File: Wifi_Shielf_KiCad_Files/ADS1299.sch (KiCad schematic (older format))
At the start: 20 parts, among them U9 ADS1299

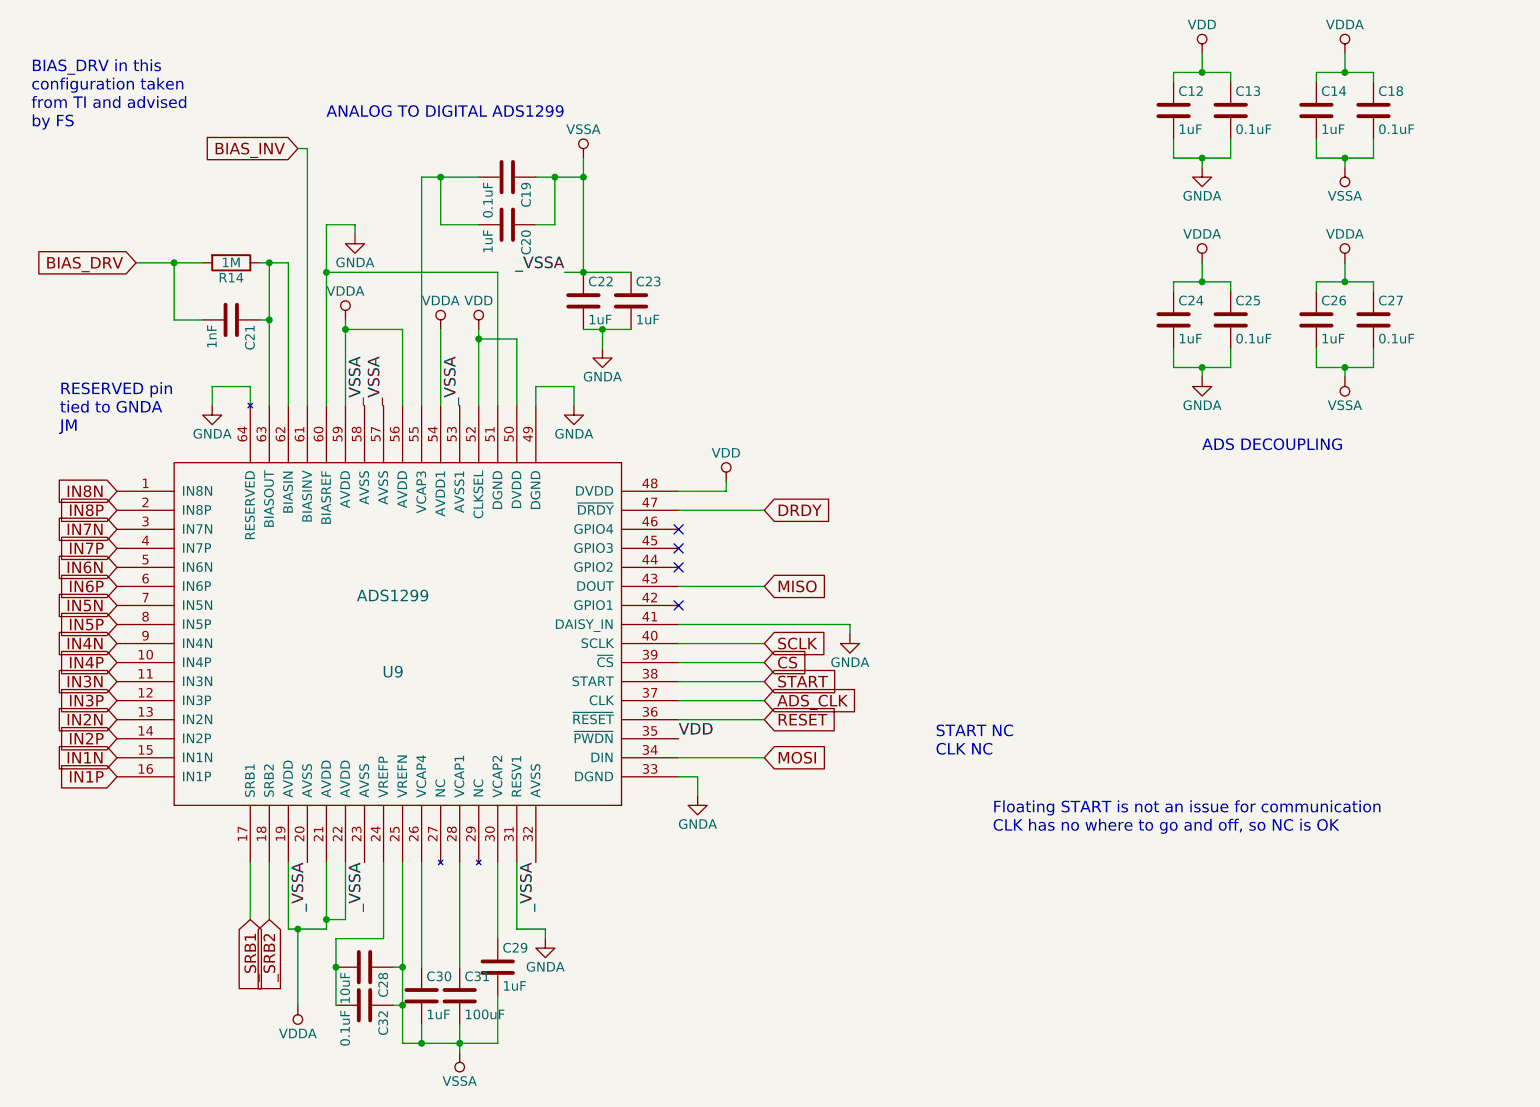
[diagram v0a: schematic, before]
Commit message: FIX: Finish DRC
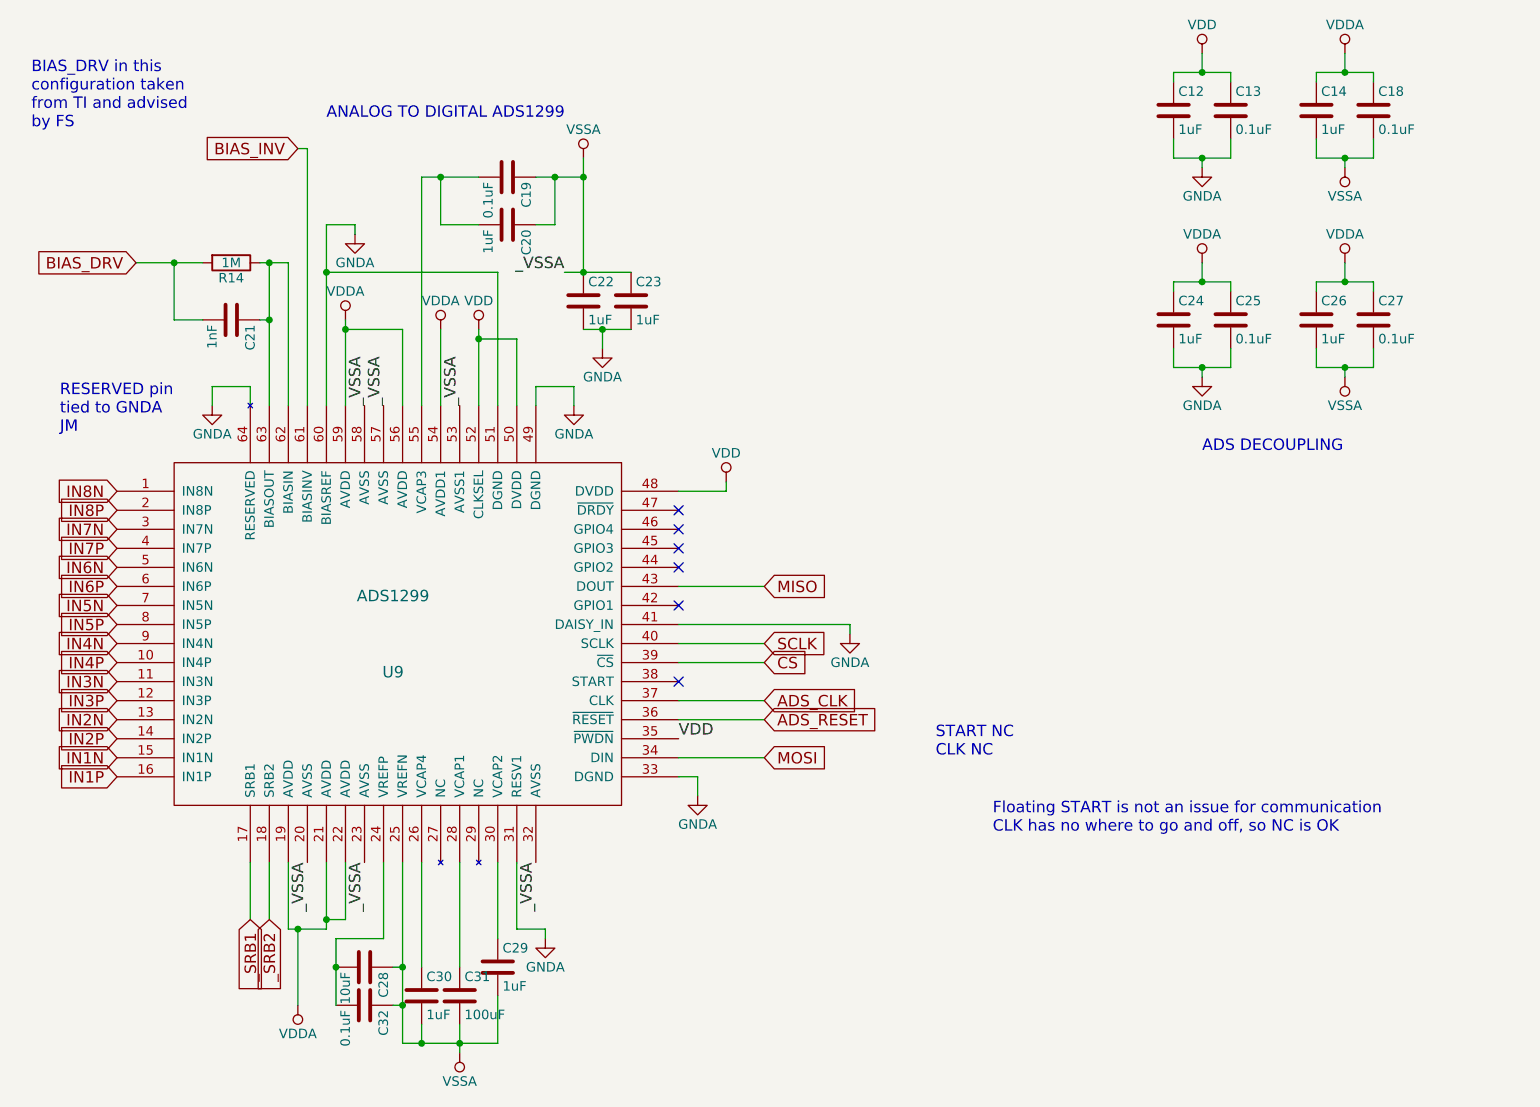
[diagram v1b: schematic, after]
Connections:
- net DRDY: no longer names the net of U9.47 (~DRDY~)
- net RESET renamed ADS_RESET
- net START: no longer names the net of U9.38 (START)
- no-connect marks 4 -> 6
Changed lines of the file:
@@
 $EndComp
 $Comp
-L GNDA #PWR36
+L GNDA #PWR031
 U 1 1 59A60DC4
 P 4050 2200
-F 0 "#PWR36" H 4050 1950 50  0001 C CNN
+F 0 "#PWR031" H 4050 1950 50  0001 C CNN
 F 1 "GNDA" H 4050 2050 50  0000 C CNN
 F 2 "" H 4050 2200 50  0000 C CNN
@@
 $EndComp
 $Comp
-L VDDA #PWR39
+L VDDA #PWR032
 U 1 1 59A60DCA
 P 4000 2650
-F 0 "#PWR39" H 4000 2500 50  0001 C CNN
+F 0 "#PWR032" H 4000 2500 50  0001 C CNN
 F 1 "VDDA" H 4000 2800 50  0000 C CNN
 F 2 "" H 4000 2650 50  0000 C CNN
@@
 $EndComp
 $Comp
-L VSSA #PWR33
+L VSSA #PWR033
 U 1 1 59A60DDE
 P 5250 1800
-F 0 "#PWR33" H 5250 1650 50  0001 C CNN
+F 0 "#PWR033" H 5250 1650 50  0001 C CNN
 F 1 "VSSA" H 5250 1950 50  0000 C CNN
 F 2 "" H 5250 1800 50  0000 C CNN
@@
 $EndComp
 $Comp
-L VDD #PWR41
+L VDD #PWR034
 U 1 1 59A60DE4
 P 4700 2700
-F 0 "#PWR41" H 4700 2550 50  0001 C CNN
+F 0 "#PWR034" H 4700 2550 50  0001 C CNN
 F 1 "VDD" H 4700 2850 50  0000 C CNN
 F 2 "" H 4700 2700 50  0000 C CNN
@@
 $EndComp
 $Comp
-L GNDA #PWR42
+L GNDA #PWR035
 U 1 1 59A60DF8
 P 5350 2800
-F 0 "#PWR42" H 5350 2550 50  0001 C CNN
+F 0 "#PWR035" H 5350 2550 50  0001 C CNN
 F 1 "GNDA" H 5350 2650 50  0000 C CNN
 F 2 "" H 5350 2800 50  0000 C CNN
@@
 _VSSA
 $Comp
-L VDDA #PWR40
+L VDDA #PWR036
 U 1 1 59A60E00
 P 4500 2700
-F 0 "#PWR40" H 4500 2550 50  0001 C CNN
+F 0 "#PWR036" H 4500 2550 50  0001 C CNN
 F 1 "VDDA" H 4500 2850 50  0000 C CNN
 F 2 "" H 4500 2700 50  0000 C CNN
@@
 $EndComp
 $Comp
-L VSSA #PWR52
+L VSSA #PWR037
 U 1 1 59A60E1E
 P 4600 6500
-F 0 "#PWR52" H 4600 6350 50  0001 C CNN
+F 0 "#PWR037" H 4600 6350 50  0001 C CNN
 F 1 "VSSA" H 4600 6650 50  0000 C CNN
 F 2 "" H 4600 6500 50  0000 C CNN
@@
 _VSSA
 Wire Wire Line
-	3900 2150 3900 2400
-Wire Wire Line
-	3900 2400 3900 3100
-Wire Wire Line
-	4000 2650 4000 2700
-Wire Wire Line
-	4000 2700 4000 3100
+	3900 2150 3900 3100
+Wire Wire Line
+	4000 2650 4000 3100
 Wire Wire Line
 	4300 3100 4300 2700
@@
 	4400 3100 4400 1900
 Wire Wire Line
-	4400 1900 4500 1900
-Wire Wire Line
-	4500 1900 4700 1900
+	4400 1900 4700 1900
 Wire Wire Line
 	4700 2150 4500 2150
@@
 Connection ~ 4500 1900
 Wire Wire Line
-	5000 1900 5100 1900
-Wire Wire Line
-	5100 1900 5250 1900
+	5000 1900 5250 1900
 Wire Wire Line
 	5000 2150 5100 2150
@@
 Connection ~ 5100 1900
 Wire Wire Line
-	4700 2700 4700 2750
-Wire Wire Line
-	4700 2750 4700 3100
+	4700 2700 4700 3100
 Wire Wire Line
 	4900 3100 4900 2750
@@
 Connection ~ 5250 1900
 Wire Wire Line
-	5250 2700 5350 2700
-Wire Wire Line
-	5350 2700 5500 2700
+	5250 2700 5500 2700
 Wire Wire Line
 	5350 2700 5350 2800
 Connection ~ 5350 2700
 Wire Wire Line
-	5250 1800 5250 1900
-Wire Wire Line
-	5250 1900 5250 2400
+	5250 1800 5250 2400
 Connection ~ 5250 2400
 Wire Wire Line
-	5150 2400 5250 2400
-Wire Wire Line
-	5250 2400 5500 2400
+	5150 2400 5500 2400
 Wire Wire Line
 	4500 3100 4500 2700
@@
 	4800 6450 4800 6200
 Wire Wire Line
-	4300 6450 4400 6450
-Wire Wire Line
-	4400 6450 4600 6450
-Wire Wire Line
-	4600 6450 4800 6450
-Wire Wire Line
-	4600 6350 4600 6450
-Wire Wire Line
-	4600 6450 4600 6500
+	4300 6450 4800 6450
+Wire Wire Line
+	4600 6350 4600 6500
 Connection ~ 4600 6450
 Wire Wire Line
@@
 	4200 5900 3950 5900
 Wire Wire Line
-	3950 5900 3950 6050
-Wire Wire Line
-	3950 6050 3950 6250
+	3950 5900 3950 6250
 Connection ~ 3950 6050
 Wire Wire Line
-	4300 5500 4300 6050
-Wire Wire Line
-	4300 6050 4300 6250
-Wire Wire Line
-	4300 6250 4300 6450
+	4300 5500 4300 6450
 Wire Wire Line
 	4300 6050 4250 6050
@@
 BIAS_DRV
 $Comp
-L GNDA #PWR46
+L GNDA #PWR038
 U 1 1 59A61175
 P 5200 3100
-F 0 "#PWR46" H 5200 2850 50  0001 C CNN
+F 0 "#PWR038" H 5200 2850 50  0001 C CNN
 F 1 "GNDA" H 5200 2950 50  0000 C CNN
 F 2 "" H 5200 3100 50  0000 C CNN
@@
 	5200 3000 5200 3100
 $Comp
-L GNDA #PWR45
+L GNDA #PWR039
 U 1 1 59A6120B
 P 3300 3100
-F 0 "#PWR45" H 3300 2850 50  0001 C CNN
+F 0 "#PWR039" H 3300 2850 50  0001 C CNN
 F 1 "GNDA" H 3300 2950 50  0000 C CNN
 F 2 "" H 3300 3100 50  0000 C CNN
@@
 Text GLabel 6200 4450 2    60   Input ~ 0
 CS
-Text GLabel 6200 4550 2    60   Input ~ 0
-START
 Text GLabel 6200 4750 2    60   Input ~ 0
-RESET
+ADS_RESET
 Text GLabel 6200 4950 2    60   Input ~ 0
 MOSI
 $Comp
-L GNDA #PWR49
+L GNDA #PWR040
 U 1 1 59A61413
 P 5850 5150
-F 0 "#PWR49" H 5850 4900 50  0001 C CNN
+F 0 "#PWR040" H 5850 4900 50  0001 C CNN
 F 1 "GNDA" H 5850 5000 50  0000 C CNN
 F 2 "" H 5850 5150 50  0000 C CNN
@@
 	6200 4750 5750 4750
 Wire Wire Line
-	6200 4550 5750 4550
-Wire Wire Line
 	6200 4450 5750 4450
 Wire Wire Line
 	6200 4350 5750 4350
 $Comp
-L GNDA #PWR48
+L GNDA #PWR041
 U 1 1 59A61697
 P 6650 4300
-F 0 "#PWR48" H 6650 4050 50  0001 C CNN
+F 0 "#PWR041" H 6650 4050 50  0001 C CNN
 F 1 "GNDA" H 6650 4150 50  0000 C CNN
 F 2 "" H 6650 4300 50  0000 C CNN
@@
 Wire Wire Line
 	6200 4050 5750 4050
-Text GLabel 6200 3650 2    60   Input ~ 0
-DRDY
-Wire Wire Line
-	6200 3650 5750 3650
-$Comp
-L VDD #PWR47
+$Comp
+L VDD #PWR042
 U 1 1 59A618D3
 P 6000 3500
-F 0 "#PWR47" H 6000 3350 50  0001 C CNN
+F 0 "#PWR042" H 6000 3350 50  0001 C CNN
 F 1 "VDD" H 6000 3650 50  0000 C CNN
 F 2 "" H 6000 3500 50  0000 C CNN
@@
 	6000 3550 5750 3550
 $Comp
-L GNDA #PWR50
+L GNDA #PWR043
 U 1 1 59A62028
 P 5050 5900
-F 0 "#PWR50" H 5050 5650 50  0001 C CNN
+F 0 "#PWR043" H 5050 5650 50  0001 C CNN
 F 1 "GNDA" H 5050 5750 50  0000 C CNN
 F 2 "" H 5050 5900 50  0000 C CNN
@@
 	4900 5850 4900 5500
 $Comp
-L VDDA #PWR51
+L VDDA #PWR044
 U 1 1 59A62102
 P 3750 6250
-F 0 "#PWR51" H 3750 6100 50  0001 C CNN
+F 0 "#PWR044" H 3750 6100 50  0001 C CNN
 F 1 "VDDA" H 3750 6400 50  0000 C CNN
 F 2 "" H 3750 6250 50  0000 C CNN
@@
 $EndComp
 Wire Wire Line
-	3900 5850 3900 5800
-Wire Wire Line
-	3900 5800 3900 5500
-Wire Wire Line
-	3700 5850 3750 5850
-Wire Wire Line
-	3750 5850 3900 5850
+	3900 5850 3900 5500
+Wire Wire Line
+	3700 5850 3900 5850
 Wire Wire Line
 	3750 5850 3750 6250
@@
 $EndComp
 $Comp
-L VDD #PWR31
+L VDD #PWR045
 U 1 1 59A62F84
 P 8500 1250
-F 0 "#PWR31" H 8500 1100 50  0001 C CNN
+F 0 "#PWR045" H 8500 1100 50  0001 C CNN
 F 1 "VDD" H 8500 1400 50  0000 C CNN
 F 2 "" H 8500 1250 50  0000 C CNN
@@
 $EndComp
 $Comp
-L GNDA #PWR34
+L GNDA #PWR046
 U 1 1 59A62F8A
 P 8500 1850
-F 0 "#PWR34" H 8500 1600 50  0001 C CNN
+F 0 "#PWR046" H 8500 1600 50  0001 C CNN
 F 1 "GNDA" H 8500 1700 50  0000 C CNN
 F 2 "" H 8500 1850 50  0000 C CNN
@@
 $EndComp
 $Comp
-L VDDA #PWR32
+L VDDA #PWR047
 U 1 1 59A62F9E
 P 9250 1250
-F 0 "#PWR32" H 9250 1100 50  0001 C CNN
+F 0 "#PWR047" H 9250 1100 50  0001 C CNN
 F 1 "VDDA" H 9250 1400 50  0000 C CNN
 F 2 "" H 9250 1250 50  0000 C CNN
@@
 $EndComp
 $Comp
-L VSSA #PWR35
+L VSSA #PWR048
 U 1 1 59A62FA4
 P 9250 1850
-F 0 "#PWR35" H 9250 1700 50  0001 C CNN
+F 0 "#PWR048" H 9250 1700 50  0001 C CNN
 F 1 "VSSA" H 9250 2000 50  0000 C CNN
 F 2 "" H 9250 1850 50  0000 C CNN
@@
 $EndComp
 $Comp
-L GNDA #PWR43
+L GNDA #PWR049
 U 1 1 59A62FB8
 P 8500 2950
-F 0 "#PWR43" H 8500 2700 50  0001 C CNN
+F 0 "#PWR049" H 8500 2700 50  0001 C CNN
 F 1 "GNDA" H 8500 2800 50  0000 C CNN
 F 2 "" H 8500 2950 50  0000 C CNN
@@
 $EndComp
 $Comp
-L VDDA #PWR38
+L VDDA #PWR050
 U 1 1 59A62FCC
 P 9250 2350
-F 0 "#PWR38" H 9250 2200 50  0001 C CNN
+F 0 "#PWR050" H 9250 2200 50  0001 C CNN
 F 1 "VDDA" H 9250 2500 50  0000 C CNN
 F 2 "" H 9250 2350 50  0000 C CNN
@@
 $EndComp
 $Comp
-L VDDA #PWR37
+L VDDA #PWR051
 U 1 1 59A62FD2
 P 8500 2350
-F 0 "#PWR37" H 8500 2200 50  0001 C CNN
+F 0 "#PWR051" H 8500 2200 50  0001 C CNN
 F 1 "VDDA" H 8500 2500 50  0000 C CNN
 F 2 "" H 8500 2350 50  0000 C CNN
@@
 	8650 1800 8650 1700
 Wire Wire Line
-	8350 1800 8500 1800
-Wire Wire Line
-	8500 1800 8650 1800
+	8350 1800 8650 1800
 Wire Wire Line
 	8500 1800 8500 1850
@@
 	8650 1350 8650 1400
 Wire Wire Line
-	8350 1350 8500 1350
-Wire Wire Line
-	8500 1350 8650 1350
+	8350 1350 8650 1350
 Wire Wire Line
 	8500 1350 8500 1250
@@
 	9400 1800 9400 1700
 Wire Wire Line
-	9100 1800 9250 1800
-Wire Wire Line
-	9250 1800 9400 1800
+	9100 1800 9400 1800
 Wire Wire Line
 	9250 1800 9250 1850
@@
 	9400 1350 9400 1400
 Wire Wire Line
-	9100 1350 9250 1350
-Wire Wire Line
-	9250 1350 9400 1350
+	9100 1350 9400 1350
 Wire Wire Line
 	9250 1350 9250 1250
@@
 	8650 2900 8650 2800
 Wire Wire Line
-	8350 2900 8500 2900
-Wire Wire Line
-	8500 2900 8650 2900
+	8350 2900 8650 2900
 Wire Wire Line
 	8500 2900 8500 2950
@@
 	8650 2450 8650 2500
 Wire Wire Line
-	8350 2450 8500 2450
-Wire Wire Line
-	8500 2450 8650 2450
+	8350 2450 8650 2450
 Wire Wire Line
 	8500 2450 8500 2350
@@
 	9400 2900 9400 2800
 Wire Wire Line
-	9100 2900 9250 2900
-Wire Wire Line
-	9250 2900 9400 2900
+	9100 2900 9400 2900
 Wire Wire Line
 	9250 2900 9250 2950
@@
 	9400 2450 9400 2500
 Wire Wire Line
-	9100 2450 9250 2450
-Wire Wire Line
-	9250 2450 9400 2450
+	9100 2450 9400 2450
 Wire Wire Line
 	9250 2450 9250 2350
@@
 Connection ~ 9250 2450
 $Comp
-L VSSA #PWR44
+L VSSA #PWR052
 U 1 1 59A63001
 P 9250 2950
-F 0 "#PWR44" H 9250 2800 50  0001 C CNN
+F 0 "#PWR052" H 9250 2800 50  0001 C CNN
 F 1 "VSSA" H 9250 3100 50  0000 C CNN
 F 2 "" H 9250 2950 50  0000 C CNN
@@
 	6200 4650 5750 4650
 Wire Wire Line
-	3600 2350 3600 2650
-Wire Wire Line
-	3600 2650 3600 3100
+	3600 2350 3600 3100
 Wire Wire Line
 	3600 2650 3550 2650
 Wire Wire Line
-	3550 2350 3600 2350
-Wire Wire Line
-	3600 2350 3700 2350
+	3550 2350 3700 2350
 Connection ~ 3600 2650
 Wire Wire Line
-	3250 2350 3100 2350
-Wire Wire Line
-	3100 2350 2900 2350
+	2900 2350 3250 2350
 Wire Wire Line
 	3250 2650 3100 2650
@@
 	0    1    1    0
 $EndComp
+NoConn ~ 5750 3650
+NoConn ~ 5750 4550
 $EndSCHEMATC
